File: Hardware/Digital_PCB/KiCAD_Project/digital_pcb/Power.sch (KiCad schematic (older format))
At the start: 19 parts, among them J5 Power, J6 Power Switch, U10 TPS793, U7 LT1521-3.3, U8 TEC 2-0921, U9 TPS723

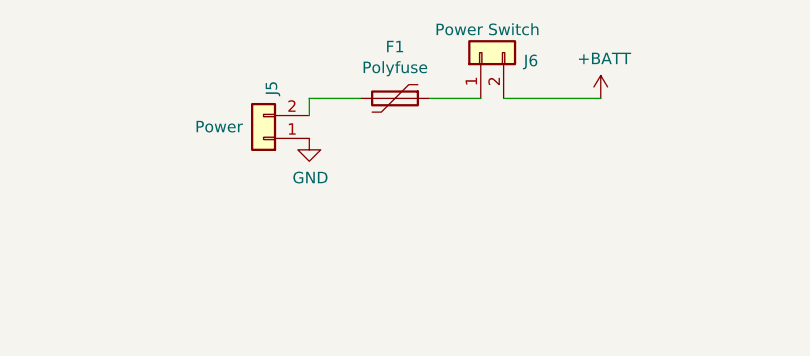
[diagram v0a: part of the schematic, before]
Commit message: Digital PCB Rev 1.0 complete.
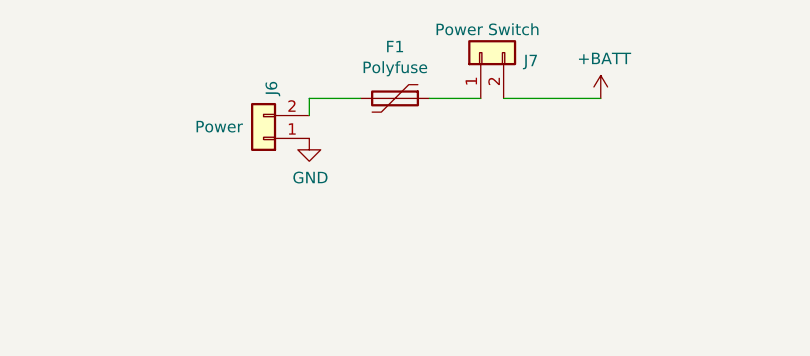
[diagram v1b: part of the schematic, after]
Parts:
- renumbered J5 to J6, J6 to J7
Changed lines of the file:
@@
 Sheet 5 5
 Title "Digital Rotating Electronics - NSSL EFM"
-Date "2019-11-26"
+Date "2019-12-30"
 Rev "1.0"
 Comp "Leeman Geophysical LLC"
@@
 $EndComp
 $Comp
-L power:+5V #PWR060
+L power:+5V #PWR070
 U 1 1 5DE8F62B
 P 4675 4775
-F 0 "#PWR060" H 4675 4625 50  0001 C CNN
+F 0 "#PWR070" H 4675 4625 50  0001 C CNN
 F 1 "+5V" V 4675 4900 50  0000 L CNN
 F 2 "" H 4675 4775 50  0001 C CNN
@@
 $EndComp
 $Comp
-L power:-5V #PWR062
+L power:-5V #PWR072
 U 1 1 5DE8F95D
 P 4675 4975
-F 0 "#PWR062" H 4675 5075 50  0001 C CNN
+F 0 "#PWR072" H 4675 5075 50  0001 C CNN
 F 1 "-5V" V 4690 5103 50  0000 L CNN
 F 2 "" H 4675 4975 50  0001 C CNN
@@
 $EndComp
 $Comp
-L power:GND #PWR061
+L power:GND #PWR071
 U 1 1 5DE8FAFE
 P 4675 4875
-F 0 "#PWR061" H 4675 4625 50  0001 C CNN
+F 0 "#PWR071" H 4675 4625 50  0001 C CNN
 F 1 "GND" V 4675 4750 50  0000 R CNN
 F 2 "" H 4675 4875 50  0001 C CNN
@@
 $EndComp
 $Comp
-L Connector_Generic:Conn_01x02 J6
+L Connector_Generic:Conn_01x02 J7
 U 1 1 5DE954BF
 P 6150 1750
-F 0 "J6" V 6114 1562 50  0000 R CNN
+F 0 "J7" V 6114 1562 50  0000 R CNN
 F 1 "Power Switch" V 6250 1950 50  0000 R CNN
 F 2 "Pin_Headers:Pin_Header_Straight_1x02_Pitch2.54mm" H 6150 1750 50  0001 C CNN
@@
 $EndComp
 $Comp
-L power:GND #PWR064
+L power:GND #PWR074
 U 1 1 5DE97A99
 P 5400 2125
-F 0 "#PWR064" H 5400 1875 50  0001 C CNN
+F 0 "#PWR074" H 5400 1875 50  0001 C CNN
 F 1 "GND" H 5405 1952 50  0000 C CNN
 F 2 "" H 5400 2125 50  0001 C CNN
@@
 	6250 1950 6675 1950
 $Comp
-L power:+BATT #PWR066
+L power:+BATT #PWR076
 U 1 1 5DE986D1
 P 6675 1950
-F 0 "#PWR066" H 6675 1800 50  0001 C CNN
+F 0 "#PWR076" H 6675 1800 50  0001 C CNN
 F 1 "+BATT" H 6690 2123 50  0000 C CNN
 F 2 "" H 6675 1950 50  0001 C CNN
@@
 $EndComp
 $Comp
-L power:+BATT #PWR057
+L power:+BATT #PWR067
 U 1 1 5DE9A4F3
 P 3100 4875
-F 0 "#PWR057" H 3100 4725 50  0001 C CNN
+F 0 "#PWR067" H 3100 4725 50  0001 C CNN
 F 1 "+BATT" H 3115 5048 50  0000 C CNN
 F 2 "" H 3100 4875 50  0001 C CNN
@@
 	3100 4875 3475 4875
 $Comp
-L power:GND #PWR058
+L power:GND #PWR068
 U 1 1 5DE9ADC2
 P 3475 4975
-F 0 "#PWR058" H 3475 4725 50  0001 C CNN
+F 0 "#PWR068" H 3475 4725 50  0001 C CNN
 F 1 "GND" H 3480 4802 50  0000 C CNN
 F 2 "" H 3475 4975 50  0001 C CNN
@@
 $EndComp
 $Comp
-L power:GND #PWR056
+L power:GND #PWR066
 U 1 1 5DE9C8C2
 P 2950 3875
-F 0 "#PWR056" H 2950 3625 50  0001 C CNN
+F 0 "#PWR066" H 2950 3625 50  0001 C CNN
 F 1 "GND" H 2955 3702 50  0000 C CNN
 F 2 "" H 2950 3875 50  0001 C CNN
@@
 	2950 3400 3325 3400
 $Comp
-L power:+BATT #PWR055
+L power:+BATT #PWR065
 U 1 1 5DE9E405
 P 2425 3400
-F 0 "#PWR055" H 2425 3250 50  0001 C CNN
+F 0 "#PWR065" H 2425 3250 50  0001 C CNN
 F 1 "+BATT" H 2440 3573 50  0000 C CNN
 F 2 "" H 2425 3400 50  0001 C CNN
@@
 Connection ~ 2575 3400
 $Comp
-L power:GND #PWR059
+L power:GND #PWR069
 U 1 1 5DE9EC09
 P 4075 4000
-F 0 "#PWR059" H 4075 3750 50  0001 C CNN
+F 0 "#PWR069" H 4075 3750 50  0001 C CNN
 F 1 "GND" H 4080 3827 50  0000 C CNN
 F 2 "" H 4075 4000 50  0001 C CNN
@@
 $EndComp
 $Comp
-L power:GND #PWR063
+L power:GND #PWR073
 U 1 1 5DEA021B
 P 5200 3875
-F 0 "#PWR063" H 5200 3625 50  0001 C CNN
+F 0 "#PWR073" H 5200 3625 50  0001 C CNN
 F 1 "GND" H 5205 3702 50  0000 C CNN
 F 2 "" H 5200 3875 50  0001 C CNN
@@
 Connection ~ 5575 3400
 $Comp
-L power:+3V3 #PWR065
+L power:+3V3 #PWR075
 U 1 1 5DEA3621
 P 5725 3400
-F 0 "#PWR065" H 5725 3250 50  0001 C CNN
+F 0 "#PWR075" H 5725 3250 50  0001 C CNN
 F 1 "+3V3" H 5740 3573 50  0000 C CNN
 F 2 "" H 5725 3400 50  0001 C CNN
@@
 $EndComp
 $Comp
-L power:-5V #PWR067
+L power:-5V #PWR077
 U 1 1 5E0AA734
 P 6875 3325
-F 0 "#PWR067" H 6875 3425 50  0001 C CNN
+F 0 "#PWR077" H 6875 3425 50  0001 C CNN
 F 1 "-5V" H 6800 3475 50  0000 L CNN
 F 2 "" H 6875 3325 50  0001 C CNN
@@
 	8575 3375 8575 3425
 $Comp
-L power:-2V5 #PWR075
+L power:-2V5 #PWR085
 U 1 1 5E0AD2AD
 P 8575 3325
-F 0 "#PWR075" H 8575 3425 50  0001 C CNN
+F 0 "#PWR085" H 8575 3425 50  0001 C CNN
 F 1 "-2V5" H 8590 3498 50  0000 C CNN
 F 2 "" H 8575 3325 50  0001 C CNN
@@
 Connection ~ 8575 3375
 $Comp
-L power:GND #PWR071
+L power:GND #PWR081
 U 1 1 5E0AE4FC
 P 7725 3925
-F 0 "#PWR071" H 7725 3675 50  0001 C CNN
+F 0 "#PWR081" H 7725 3675 50  0001 C CNN
 F 1 "GND" H 7730 3752 50  0000 C CNN
 F 2 "" H 7725 3925 50  0001 C CNN
@@
 $EndComp
 $Comp
-L power:GND #PWR068
+L power:GND #PWR078
 U 1 1 5E0AED71
 P 6875 3725
-F 0 "#PWR068" H 6875 3475 50  0001 C CNN
+F 0 "#PWR078" H 6875 3475 50  0001 C CNN
 F 1 "GND" H 6880 3552 50  0000 C CNN
 F 2 "" H 6875 3725 50  0001 C CNN
@@
 $EndComp
 $Comp
-L power:GND #PWR073
+L power:GND #PWR083
 U 1 1 5E0AF137
 P 8175 3775
-F 0 "#PWR073" H 8175 3525 50  0001 C CNN
+F 0 "#PWR083" H 8175 3525 50  0001 C CNN
 F 1 "GND" H 8180 3602 50  0000 C CNN
 F 2 "" H 8175 3775 50  0001 C CNN
@@
 $EndComp
 $Comp
-L power:GND #PWR076
+L power:GND #PWR086
 U 1 1 5E0AF4E6
 P 8575 3725
-F 0 "#PWR076" H 8575 3475 50  0001 C CNN
+F 0 "#PWR086" H 8575 3475 50  0001 C CNN
 F 1 "GND" H 8580 3552 50  0000 C CNN
 F 2 "" H 8575 3725 50  0001 C CNN
@@
 $EndComp
 $Comp
-L power:+5V #PWR069
+L power:+5V #PWR079
 U 1 1 5E0B6019
 P 6875 4550
-F 0 "#PWR069" H 6875 4400 50  0001 C CNN
+F 0 "#PWR079" H 6875 4400 50  0001 C CNN
 F 1 "+5V" H 6800 4700 50  0000 L CNN
 F 2 "" H 6875 4550 50  0001 C CNN
@@
 $EndComp
 $Comp
-L power:+2V5 #PWR077
+L power:+2V5 #PWR087
 U 1 1 5E0B7208
 P 8575 4550
-F 0 "#PWR077" H 8575 4400 50  0001 C CNN
+F 0 "#PWR087" H 8575 4400 50  0001 C CNN
 F 1 "+2V5" H 8590 4723 50  0000 C CNN
 F 2 "" H 8575 4550 50  0001 C CNN
@@
 $EndComp
 $Comp
-L power:GND #PWR072
+L power:GND #PWR082
 U 1 1 5E0B7D93
 P 7725 5150
-F 0 "#PWR072" H 7725 4900 50  0001 C CNN
+F 0 "#PWR082" H 7725 4900 50  0001 C CNN
 F 1 "GND" H 7730 4977 50  0000 C CNN
 F 2 "" H 7725 5150 50  0001 C CNN
@@
 $EndComp
 $Comp
-L power:GND #PWR074
+L power:GND #PWR084
 U 1 1 5E0B8400
 P 8175 5000
-F 0 "#PWR074" H 8175 4750 50  0001 C CNN
+F 0 "#PWR084" H 8175 4750 50  0001 C CNN
 F 1 "GND" H 8180 4827 50  0000 C CNN
 F 2 "" H 8175 5000 50  0001 C CNN
@@
 $EndComp
 $Comp
-L power:GND #PWR078
+L power:GND #PWR088
 U 1 1 5E0B886C
 P 8575 4950
-F 0 "#PWR078" H 8575 4700 50  0001 C CNN
+F 0 "#PWR088" H 8575 4700 50  0001 C CNN
 F 1 "GND" H 8580 4777 50  0000 C CNN
 F 2 "" H 8575 4950 50  0001 C CNN
@@
 $EndComp
 $Comp
-L power:GND #PWR070
+L power:GND #PWR080
 U 1 1 5E0B8AAB
 P 6875 4950
-F 0 "#PWR070" H 6875 4700 50  0001 C CNN
+F 0 "#PWR080" H 6875 4700 50  0001 C CNN
 F 1 "GND" H 6880 4777 50  0000 C CNN
 F 2 "" H 6875 4950 50  0001 C CNN
@@
 Connection ~ 8575 4600
 $Comp
-L Connector_Generic:Conn_01x02 J5
+L Connector_Generic:Conn_01x02 J6
 U 1 1 5E138DD7
 P 5200 2125
-F 0 "J5" V 5164 1937 50  0000 R CNN
+F 0 "J6" V 5164 1937 50  0000 R CNN
 F 1 "Power" H 5500 2075 50  0000 R CNN
 F 2 "Pin_Headers:Pin_Header_Straight_1x02_Pitch2.54mm" H 5200 2125 50  0001 C CNN

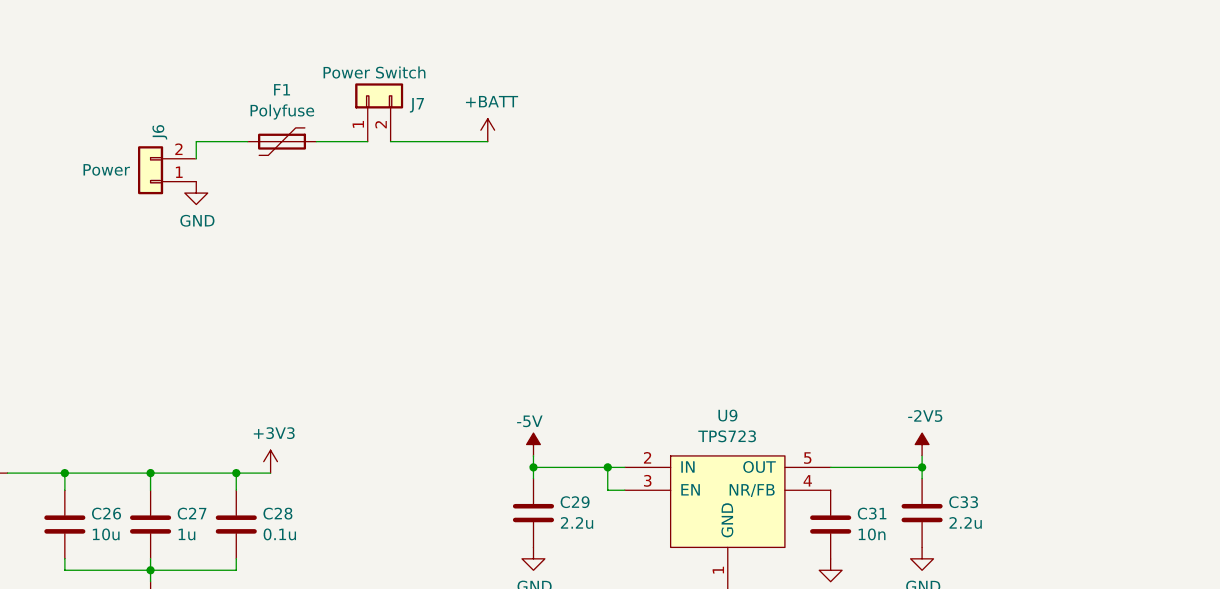
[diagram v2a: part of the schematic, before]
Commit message: Debounce power switch with load switch and RC timer. Closes #1.
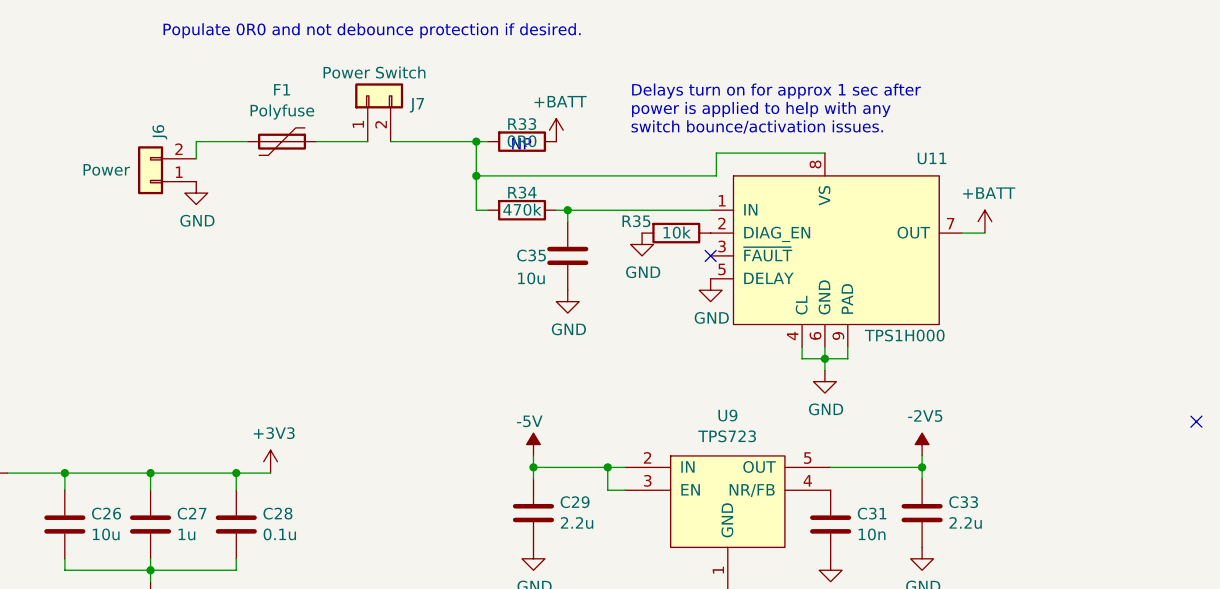
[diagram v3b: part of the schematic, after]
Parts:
- added C35: 10u, Capacitor_SMD:C_0805_2012Metric_Pad1.15x1.40mm_HandSolder, symbol Device:C
- added R33: 0R0, Resistor_SMD:R_0603_1608Metric_Pad1.05x0.95mm_HandSolder, symbol Device:R
- added R34: 470k, Resistor_SMD:R_0603_1608Metric_Pad1.05x0.95mm_HandSolder, symbol Device:R
- added R35: 10k, Resistor_SMD:R_0603_1608Metric_Pad1.05x0.95mm_HandSolder, symbol Device:R
- added U11: TPS1H000, Package_SO:MSOP-8-1EP_3x3mm_P0.65mm_EP1.95x2.15mm, symbol lib_sch:TPS1H000
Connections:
- net +BATT: now also R33.1, U11.7 (OUT); no longer J7.2 (Pin_2)
- net GND: now also C35.2, R35.2, U11.4 (CL), U11.5 (DELAY), U11.6 (GND), U11.9 (PAD)
- new net: J7.2 (Pin_2), R33.2, R34.2, U11.8 (VS)
- new net: C35.1, R34.1, U11.1 (IN)
- new net: R35.1, U11.2 (DIAG_EN)
- no-connect marks 1 -> 3
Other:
- note added: "Delays turn on for approx 1 sec after\npower is applied to help with any\nswitch bounce/activation issues."
- note added: "NP"
- note added: "Populate 0R0 and not debounce protection if desired."
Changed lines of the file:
@@
 	5925 1950 6150 1950
 Wire Wire Line
-	6250 1950 6675 1950
+	6250 1950 6625 1950
 $Comp
 L power:+BATT #PWR076
 U 1 1 5DE986D1
-P 6675 1950
-F 0 "#PWR076" H 6675 1800 50  0001 C CNN
-F 1 "+BATT" H 6690 2123 50  0000 C CNN
-F 2 "" H 6675 1950 50  0001 C CNN
-F 3 "" H 6675 1950 50  0001 C CNN
-	1    6675 1950
+P 8850 2350
+F 0 "#PWR076" H 8850 2200 50  0001 C CNN
+F 1 "+BATT" H 8865 2523 50  0000 C CNN
+F 2 "" H 8850 2350 50  0001 C CNN
+F 3 "" H 8850 2350 50  0001 C CNN
+	1    8850 2350
 	1    0    0    -1
 $EndComp
@@
 Wire Wire Line
 	5400 1950 5400 2025
+$Comp
+L Device:R R33
+U 1 1 5E84B29F
+P 6825 1950
+F 0 "R33" V 6750 1950 50  0000 C CNN
+F 1 "0R0" V 6825 1950 50  0000 C CNN
+F 2 "Resistor_SMD:R_0603_1608Metric_Pad1.05x0.95mm_HandSolder" V 6755 1950 50  0001 C CNN
+F 3 "~" H 6825 1950 50  0001 C CNN
+F 4 "1-0000006" H 6825 1950 50  0001 C CNN "Internal Part Number"
+F 5 "0" H 6825 1950 50  0001 C CNN "Populated"
+	1    6825 1950
+	0    1    1    0
+$EndComp
+Text Notes 6775 2000 0    50   ~ 0
+NP
+Text Notes 5250 1500 0    50   ~ 0
+Populate 0R0 and not debounce protection if desired.
+$Comp
+L Device:R R34
+U 1 1 5E84C312
+P 6825 2250
+F 0 "R34" V 6750 2250 50  0000 C CNN
+F 1 "470k" V 6825 2250 50  0000 C CNN
+F 2 "Resistor_SMD:R_0603_1608Metric_Pad1.05x0.95mm_HandSolder" V 6755 2250 50  0001 C CNN
+F 3 "~" H 6825 2250 50  0001 C CNN
+F 4 "1-0000068" H 6825 2250 50  0001 C CNN "Internal Part Number"
+F 5 "1" H 6825 2250 50  0001 C CNN "Populated"
+	1    6825 2250
+	0    1    1    0
+$EndComp
+Connection ~ 6625 1950
+Wire Wire Line
+	6625 1950 6675 1950
+$Comp
+L lib_sch:TPS1H000 U11
+U 1 1 5E84F128
+P 8200 2400
+F 0 "U11" H 8550 2775 50  0000 L CNN
+F 1 "TPS1H000" H 8325 2000 50  0000 L CNN
+F 2 "Package_SO:MSOP-8-1EP_3x3mm_P0.65mm_EP1.95x2.15mm" H 8150 2550 50  0001 C CNN
+F 3 "" H 8150 2550 50  0001 C CNN
+F 4 "1-0000576" H 8200 2400 50  0001 C CNN "Internal Part Number"
+F 5 "1" H 8200 2400 50  0001 C CNN "Populated"
+	1    8200 2400
+	1    0    0    -1
+$EndComp
+Wire Wire Line
+	8850 2350 8750 2350
+$Comp
+L power:+BATT #PWR089
+U 1 1 5E8529F1
+P 6975 1950
+F 0 "#PWR089" H 6975 1800 50  0001 C CNN
+F 1 "+BATT" H 6990 2123 50  0000 C CNN
+F 2 "" H 6975 1950 50  0001 C CNN
+F 3 "" H 6975 1950 50  0001 C CNN
+	1    6975 1950
+	1    0    0    -1
+$EndComp
+Wire Wire Line
+	8150 2000 7675 2000
+$Comp
+L power:GND #PWR093
+U 1 1 5E854618
+P 8150 2950
+F 0 "#PWR093" H 8150 2700 50  0001 C CNN
+F 1 "GND" H 8155 2777 50  0000 C CNN
+F 2 "" H 8150 2950 50  0001 C CNN
+F 3 "" H 8150 2950 50  0001 C CNN
+	1    8150 2950
+	1    0    0    -1
+$EndComp
+Wire Wire Line
+	8050 2900 8150 2900
+Wire Wire Line
+	8250 2900 8250 2850
+Wire Wire Line
+	8050 2850 8050 2900
+Wire Wire Line
+	8150 2850 8150 2900
+Connection ~ 8150 2900
+Wire Wire Line
+	8150 2900 8250 2900
+Wire Wire Line
+	8150 2950 8150 2900
+$Comp
+L power:GND #PWR092
+U 1 1 5E858921
+P 7650 2550
+F 0 "#PWR092" H 7650 2300 50  0001 C CNN
+F 1 "GND" H 7655 2377 50  0000 C CNN
+F 2 "" H 7650 2550 50  0001 C CNN
+F 3 "" H 7650 2550 50  0001 C CNN
+	1    7650 2550
+	1    0    0    -1
+$EndComp
+NoConn ~ 7650 2450
+NoConn ~ 9775 3175
+$Comp
+L Device:R R35
+U 1 1 5E85A986
+P 7500 2350
+F 0 "R35" V 7450 2175 50  0000 C CNN
+F 1 "10k" V 7500 2350 50  0000 C CNN
+F 2 "Resistor_SMD:R_0603_1608Metric_Pad1.05x0.95mm_HandSolder" V 7430 2350 50  0001 C CNN
+F 3 "~" H 7500 2350 50  0001 C CNN
+F 4 "1-0000010" H 7500 2350 50  0001 C CNN "Internal Part Number"
+F 5 "1" H 7500 2350 50  0001 C CNN "Populated"
+	1    7500 2350
+	0    1    1    0
+$EndComp
+$Comp
+L power:GND #PWR091
+U 1 1 5E85AE19
+P 7350 2350
+F 0 "#PWR091" H 7350 2100 50  0001 C CNN
+F 1 "GND" H 7355 2177 50  0000 C CNN
+F 2 "" H 7350 2350 50  0001 C CNN
+F 3 "" H 7350 2350 50  0001 C CNN
+	1    7350 2350
+	1    0    0    -1
+$EndComp
+Wire Wire Line
+	6975 2250 7025 2250
+Wire Wire Line
+	7025 2250 7025 2300
+$Comp
+L power:GND #PWR090
+U 1 1 5E85F585
+P 7025 2600
+F 0 "#PWR090" H 7025 2350 50  0001 C CNN
+F 1 "GND" H 7030 2427 50  0000 C CNN
+F 2 "" H 7025 2600 50  0001 C CNN
+F 3 "" H 7025 2600 50  0001 C CNN
+	1    7025 2600
+	1    0    0    -1
+$EndComp
+Wire Wire Line
+	7025 2250 7650 2250
+Connection ~ 7025 2250
+Wire Wire Line
+	6675 2250 6625 2250
+Wire Wire Line
+	6625 1950 6625 2100
+Wire Wire Line
+	6625 2100 7675 2100
+Wire Wire Line
+	7675 2100 7675 2000
+Connection ~ 6625 2100
+Wire Wire Line
+	6625 2100 6625 2250
+Text Notes 7300 1925 0    50   ~ 0
+Delays turn on for approx 1 sec after\npower is applied to help with any\nswitch bounce/activation issues.
+$Comp
+L Device:C C35
+U 1 1 5E86633E
+P 7025 2450
+F 0 "C35" H 6800 2450 50  0000 L CNN
+F 1 "10u" H 6800 2350 50  0000 L CNN
+F 2 "Capacitor_SMD:C_0805_2012Metric_Pad1.15x1.40mm_HandSolder" H 7063 2300 50  0001 C CNN
+F 3 "~" H 7025 2450 50  0001 C CNN
+F 4 "1-0000075" H 7025 2450 50  0001 C CNN "Internal Part Number"
+F 5 "1" H 7025 2450 50  0001 C CNN "Populated"
+	1    7025 2450
+	1    0    0    -1
+$EndComp
 $EndSCHEMATC

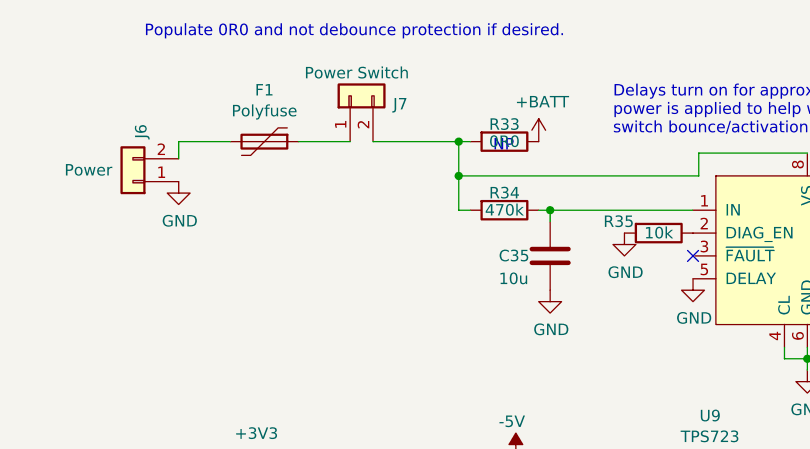
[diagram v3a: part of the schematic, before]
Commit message: Fixup DRC issues.
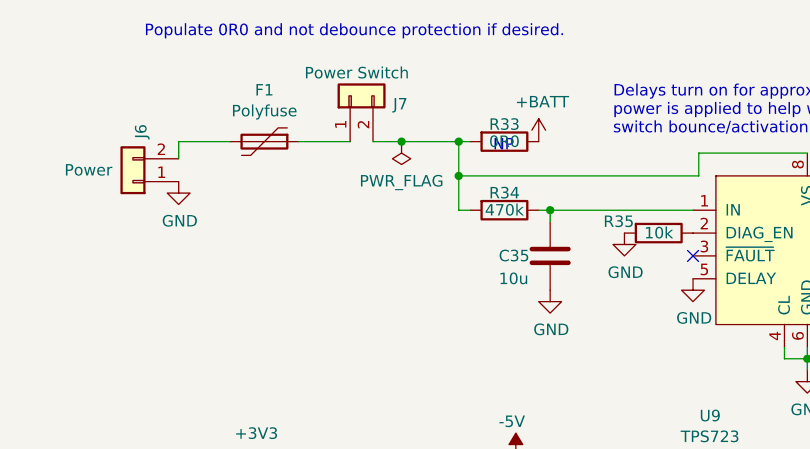
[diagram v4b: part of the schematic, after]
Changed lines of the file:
@@
 	5925 1950 6150 1950
 Wire Wire Line
-	6250 1950 6625 1950
+	6250 1950 6375 1950
 $Comp
 L power:+BATT #PWR076
@@
 	1    0    0    -1
 $EndComp
+$Comp
+L power:PWR_FLAG #FLG0101
+U 1 1 5E880B05
+P 6375 1950
+F 0 "#FLG0101" H 6375 2025 50  0001 C CNN
+F 1 "PWR_FLAG" H 6375 2123 50  0000 C CNN
+F 2 "" H 6375 1950 50  0001 C CNN
+F 3 "~" H 6375 1950 50  0001 C CNN
+	1    6375 1950
+	-1   0    0    1
+$EndComp
+Connection ~ 6375 1950
+Wire Wire Line
+	6375 1950 6625 1950
 $EndSCHEMATC
